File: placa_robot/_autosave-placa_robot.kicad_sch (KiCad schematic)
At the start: 16 parts, among them IC1 MSP430FR2355TPT, J1 conn_DFrobot, J3 Conn_02x04_Odd_Even, Y1 Crystal

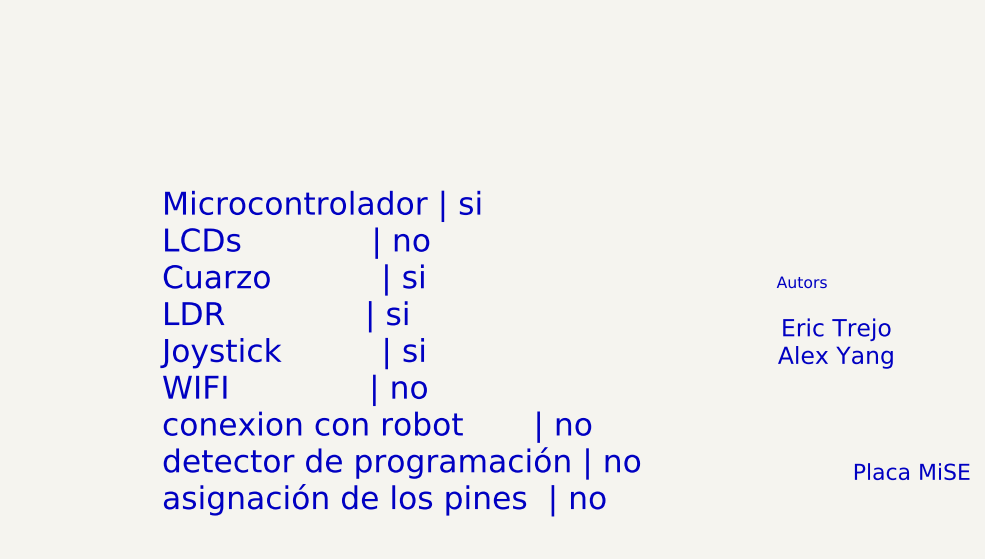
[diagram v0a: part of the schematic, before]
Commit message: Connector_robot_sensor
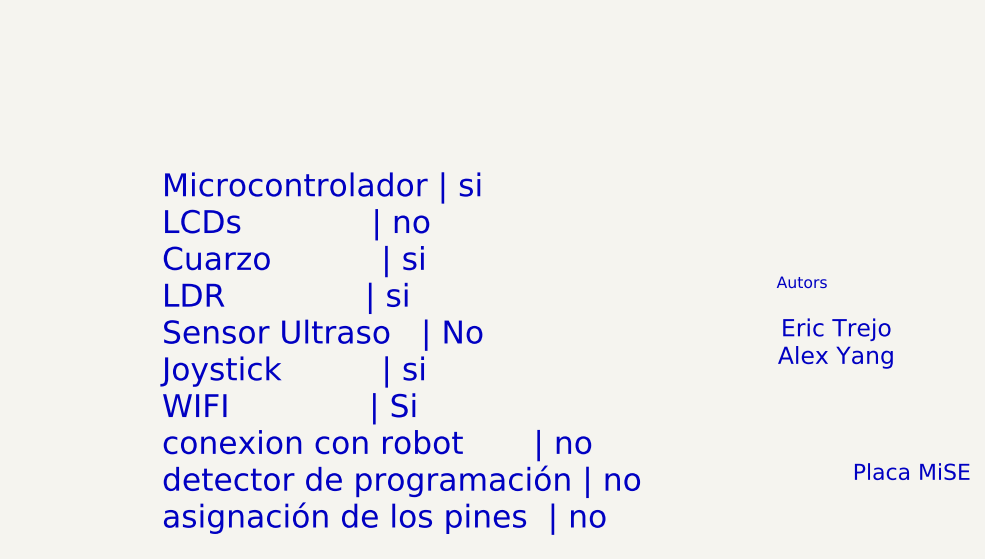
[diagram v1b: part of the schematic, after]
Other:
- note added: "Microcontrolador | si LCDs | no Cuarzo | si️ LDR | si Sensor Ultraso | No Joystick | si WIFI | Si conexion con robot | no detector de programación | no asignación de los pines | no"
- note removed: "Microcontrolador | si LCDs | no Cuarzo | si️ LDR | si Joystick | si WIFI | no conexion con robot | no detector de programación | no asignación de los pines | no"
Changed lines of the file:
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@@
 		)
 	)
-	(text "Microcontrolador | si\nLCDs             | no\nCuarzo           | si️\nLDR              | si\nJoystick          | si\nWIFI              | no\nconexion con robot       | no\ndetector de programación | no\nasignación de los pines  | no\n"
+	(text "Microcontrolador | si\nLCDs             | no\nCuarzo           | si️\nLDR              | si\nSensor Ultraso   | No\nJoystick          | si\nWIFI              | Si\nconexion con robot       | no\ndetector de programación | no\nasignación de los pines  | no\n"
 		(exclude_from_sim no)
 		(at 233.934 263.144 0)
